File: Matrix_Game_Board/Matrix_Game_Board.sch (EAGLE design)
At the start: 53 parts, among them J1 AVR_SPI_PRG_6NS, J2 AVR_SPI_PRG_6NS, J3 AVR_SPI_PRG_6NS, J4 AVR_SPI_PRG_6NS

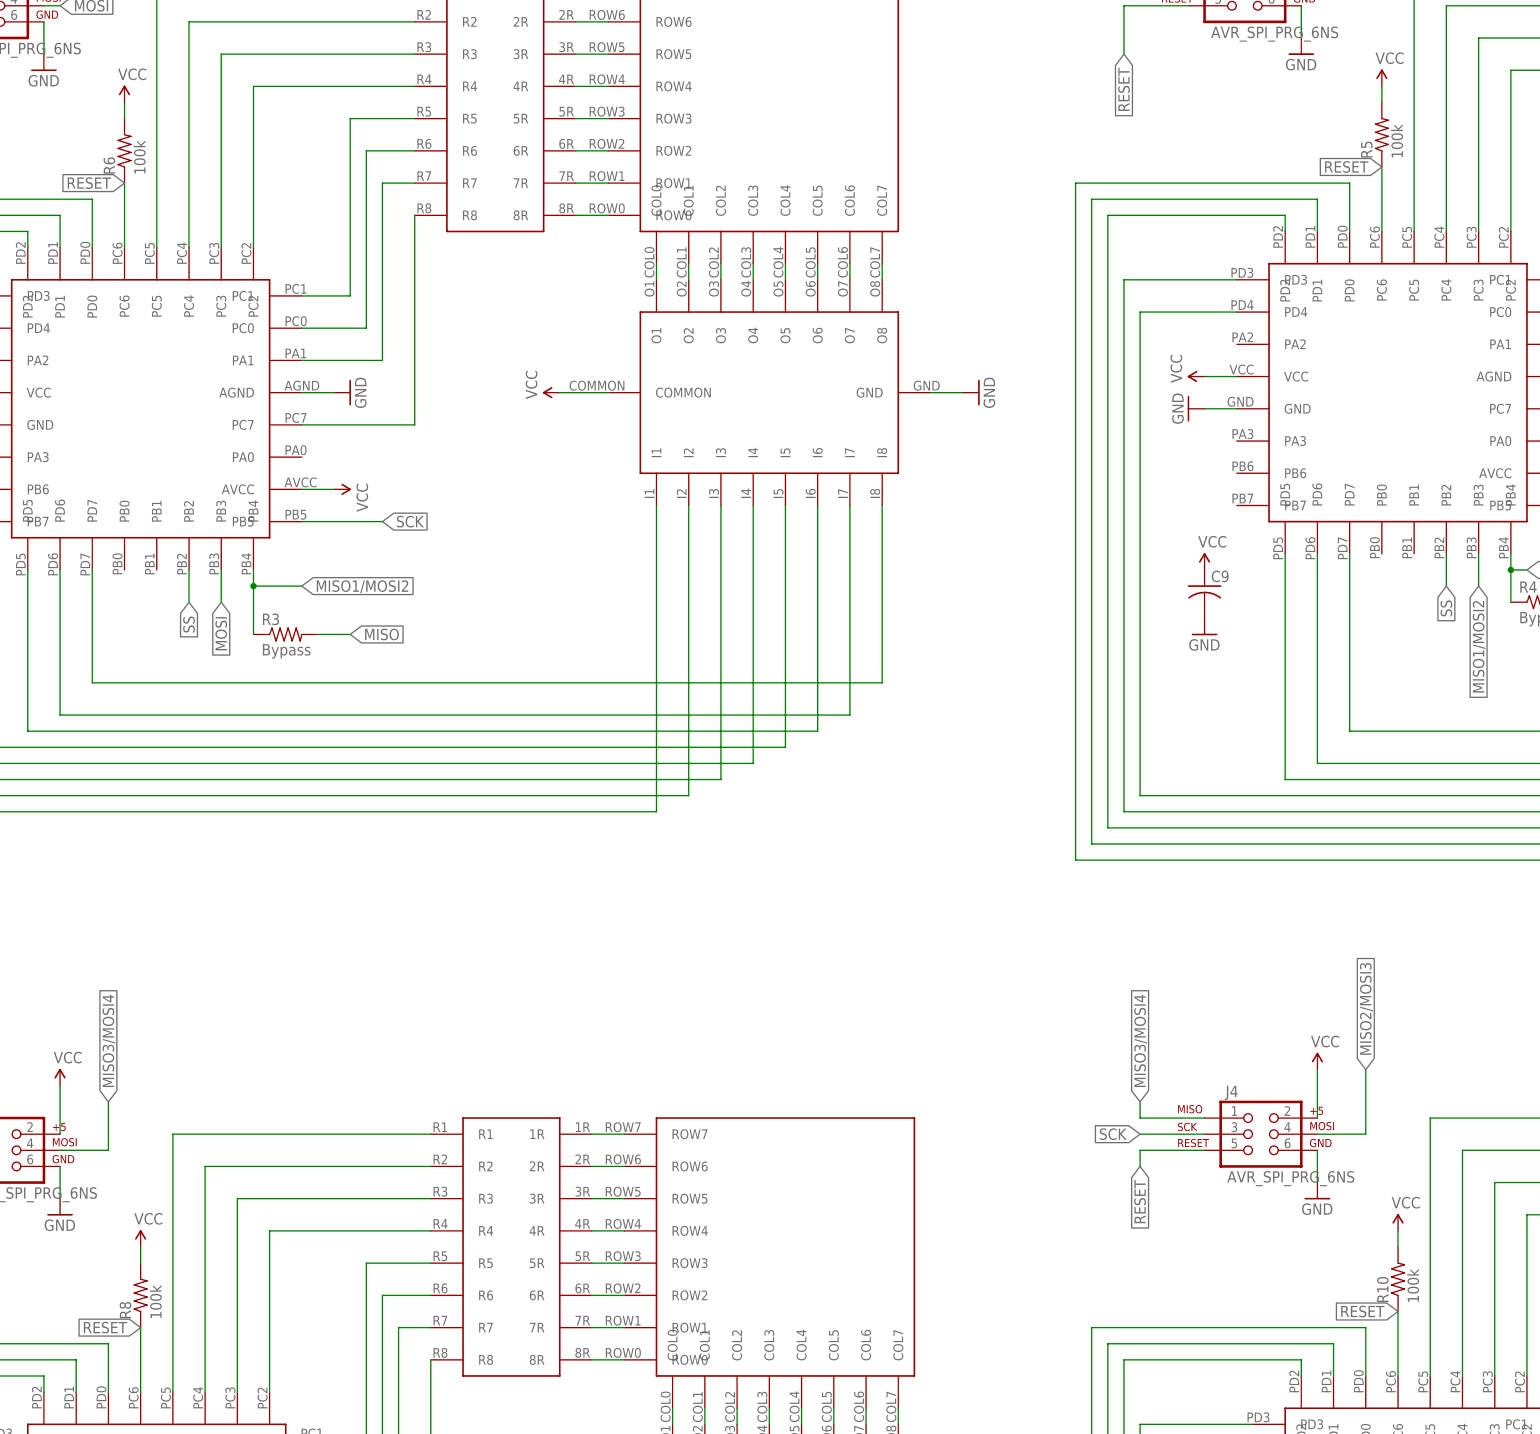
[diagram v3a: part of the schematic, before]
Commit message: Changed resistors to 0603 on gamer PCB
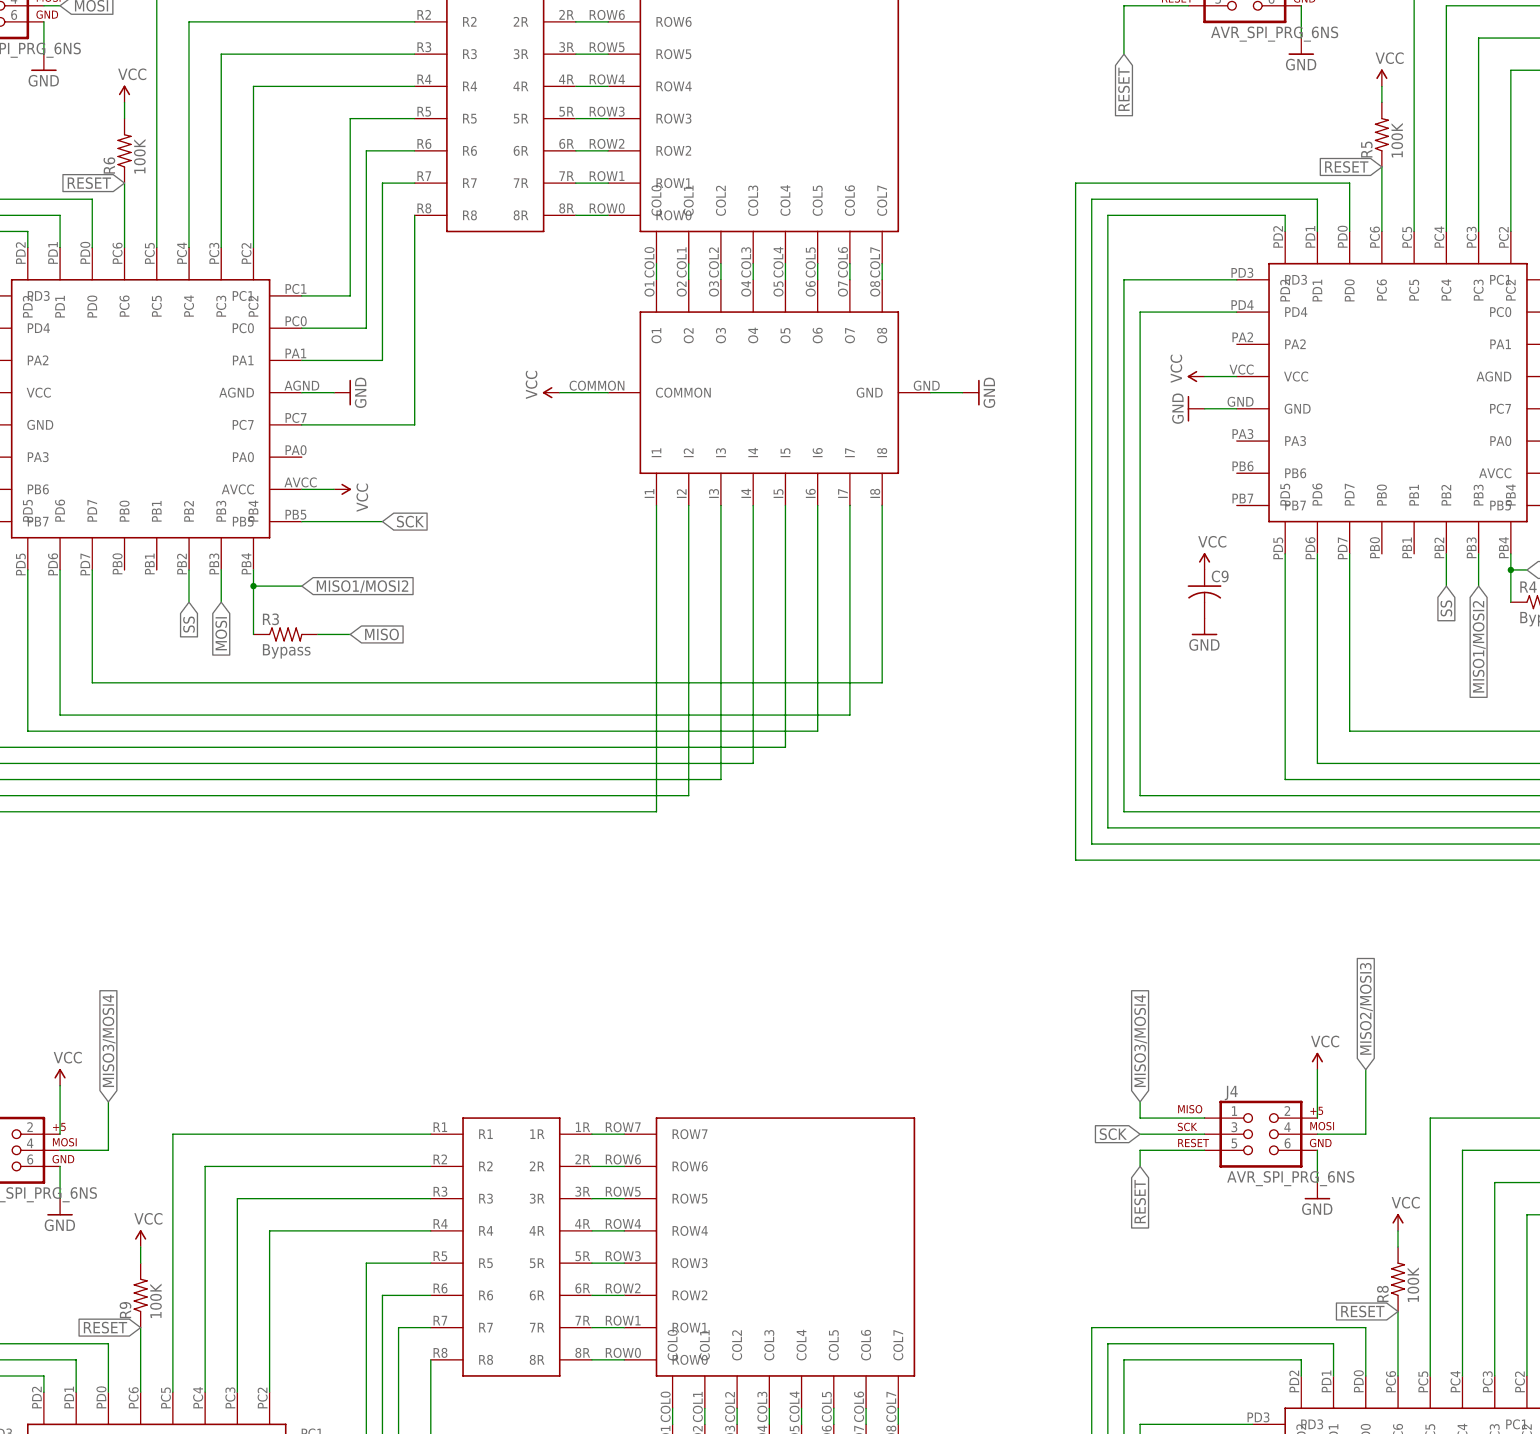
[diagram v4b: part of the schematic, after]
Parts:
- removed R10: 100k, resistor:R-US_R0805
- added R9: 100K, resistor:R-US_R0603
- R3, R4: device resistor:R-US_R0805 -> resistor:R-US_R0603
- R5, R6, R8: value 100k -> 100K; device resistor:R-US_R0805 -> resistor:R-US_R0603
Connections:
- net RESET: now also R9.1; no longer R10.1
- net VCC: now also R9.2; no longer R10.2
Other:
- moved on the sheet: R8
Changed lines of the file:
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@@
 <part name="GND23" library="SparkFun-Aesthetics" deviceset="GND" device=""/>
 <part name="GND26" library="SparkFun-Aesthetics" deviceset="GND" device=""/>
-<part name="R3" library="resistor" deviceset="R-US_" device="R0805" value="Bypass"/>
-<part name="R6" library="resistor" deviceset="R-US_" device="R0805" value="100k"/>
 <part name="SUPPLY22" library="SparkFun-Aesthetics" deviceset="VCC" device=""/>
 <part name="U$25" library="ScottSilver" deviceset="LM386" device=""/>
@@
 <part name="GND8" library="SparkFun-Aesthetics" deviceset="GND" device=""/>
 <part name="SUPPLY8" library="SparkFun-Aesthetics" deviceset="VCC" device=""/>
-<part name="R4" library="resistor" deviceset="R-US_" device="R0805" value="Bypass"/>
-<part name="R5" library="resistor" deviceset="R-US_" device="R0805" value="100k"/>
 <part name="SUPPLY9" library="SparkFun-Aesthetics" deviceset="VCC" device=""/>
 <part name="U$8" library="ScottSilver" deviceset="8X8_LED_MATRIX" device=""/>
@@
 <part name="GND12" library="SparkFun-Aesthetics" deviceset="GND" device=""/>
 <part name="SUPPLY13" library="SparkFun-Aesthetics" deviceset="VCC" device=""/>
-<part name="R8" library="resistor" deviceset="R-US_" device="R0805" value="100k"/>
 <part name="SUPPLY14" library="SparkFun-Aesthetics" deviceset="VCC" device=""/>
 <part name="U$13" library="ScottSilver" deviceset="8X8_LED_MATRIX" device=""/>
@@
 <part name="GND16" library="SparkFun-Aesthetics" deviceset="GND" device=""/>
 <part name="SUPPLY24" library="SparkFun-Aesthetics" deviceset="VCC" device=""/>
-<part name="R10" library="resistor" deviceset="R-US_" device="R0805" value="100k"/>
 <part name="SUPPLY25" library="SparkFun-Aesthetics" deviceset="VCC" device=""/>
 <part name="GND32" library="SparkFun-Aesthetics" deviceset="GND" device=""/>
@@
 <part name="GND38" library="SparkFun-Aesthetics" deviceset="GND" device=""/>
 <part name="GND39" library="SparkFun-Aesthetics" deviceset="GND" device=""/>
+<part name="R3" library="resistor" deviceset="R-US_" device="R0603" value="Bypass"/>
+<part name="R4" library="resistor" deviceset="R-US_" device="R0603" value="Bypass"/>
+<part name="R6" library="resistor" deviceset="R-US_" device="R0603" value="100K"/>
+<part name="R5" library="resistor" deviceset="R-US_" device="R0603" value="100K"/>
+<part name="R8" library="resistor" deviceset="R-US_" device="R0603" value="100K"/>
+<part name="R9" library="resistor" deviceset="R-US_" device="R0603" value="100K"/>
 </parts>
 <sheets>
@@
 <instance part="GND23" gate="1" x="215.9" y="-33.02"/>
 <instance part="GND26" gate="1" x="398.78" y="10.16" rot="MR90"/>
-<instance part="R3" gate="G$1" x="106.68" y="271.78"/>
-<instance part="R6" gate="G$1" x="81.28" y="347.98" rot="R90"/>
 <instance part="SUPPLY22" gate="G$1" x="81.28" y="355.6"/>
 <instance part="U$25" gate="G$1" x="477.52" y="182.88"/>
@@
 <instance part="GND8" gate="1" x="266.7" y="363.22"/>
 <instance part="SUPPLY8" gate="G$1" x="266.7" y="383.54"/>
-<instance part="R4" gate="G$1" x="304.8" y="276.86"/>
-<instance part="R5" gate="G$1" x="279.4" y="350.52" rot="R90"/>
 <instance part="SUPPLY9" gate="G$1" x="279.4" y="358.14"/>
 <instance part="U$8" gate="G$1" x="185.42" y="175.26"/>
@@
 <instance part="GND12" gate="1" x="71.12" y="180.34"/>
 <instance part="SUPPLY13" gate="G$1" x="71.12" y="200.66"/>
-<instance part="R8" gate="G$1" x="83.82" y="167.64" rot="R90"/>
 <instance part="SUPPLY14" gate="G$1" x="83.82" y="175.26"/>
 <instance part="U$13" gate="G$1" x="383.54" y="177.8"/>
@@
 <instance part="GND16" gate="1" x="269.24" y="182.88"/>
 <instance part="SUPPLY24" gate="G$1" x="269.24" y="203.2"/>
-<instance part="R10" gate="G$1" x="281.94" y="170.18" rot="R90"/>
 <instance part="SUPPLY25" gate="G$1" x="281.94" y="177.8"/>
 <instance part="GND32" gate="1" x="452.12" y="27.94" rot="R270"/>
@@
 <instance part="GND38" gate="1" x="436.88" y="-55.88"/>
 <instance part="GND39" gate="1" x="436.88" y="-81.28"/>
+<instance part="R3" gate="G$1" x="106.68" y="271.78"/>
+<instance part="R4" gate="G$1" x="304.8" y="276.86"/>
+<instance part="R6" gate="G$1" x="81.28" y="347.98" rot="R90"/>
+<instance part="R5" gate="G$1" x="279.4" y="350.52" rot="R90"/>
+<instance part="R8" gate="G$1" x="281.94" y="170.18" rot="R90"/>
+<instance part="R9" gate="G$1" x="83.82" y="167.64" rot="R90"/>
 </instances>
 <busses>
@@
 </segment>
 <segment>
-<pinref part="R6" gate="G$1" pin="2"/>
 <pinref part="SUPPLY22" gate="G$1" pin="VCC"/>
 <wire x1="81.28" y1="355.6" x2="81.28" y2="353.06" width="0.1524" layer="91"/>
+<pinref part="R6" gate="G$1" pin="2"/>
 </segment>
 <segment>
@@
 </segment>
 <segment>
-<pinref part="R5" gate="G$1" pin="2"/>
 <pinref part="SUPPLY9" gate="G$1" pin="VCC"/>
 <wire x1="279.4" y1="358.14" x2="279.4" y2="355.6" width="0.1524" layer="91"/>
+<pinref part="R5" gate="G$1" pin="2"/>
 </segment>
 <segment>
@@
 </segment>
 <segment>
-<pinref part="R8" gate="G$1" pin="2"/>
 <pinref part="SUPPLY14" gate="G$1" pin="VCC"/>
 <wire x1="83.82" y1="175.26" x2="83.82" y2="172.72" width="0.1524" layer="91"/>
+<pinref part="R9" gate="G$1" pin="2"/>
 </segment>
 <segment>
@@
 </segment>
 <segment>
-<pinref part="R10" gate="G$1" pin="2"/>
 <pinref part="SUPPLY25" gate="G$1" pin="VCC"/>
 <wire x1="281.94" y1="177.8" x2="281.94" y2="175.26" width="0.1524" layer="91"/>
+<pinref part="R8" gate="G$1" pin="2"/>
 </segment>
 <segment>
@@
 <wire x1="83.82" y1="152.4" x2="83.82" y2="162.56" width="0.1524" layer="91"/>
 <label x="83.82" y="162.56" size="1.778" layer="95" rot="R180" xref="yes"/>
-<pinref part="R8" gate="G$1" pin="1"/>
+<pinref part="R9" gate="G$1" pin="1"/>
 </segment>
 <segment>
@@
 <wire x1="281.94" y1="154.94" x2="281.94" y2="165.1" width="0.1524" layer="91"/>
 <label x="281.94" y="165.1" size="1.778" layer="95" rot="R180" xref="yes"/>
-<pinref part="R10" gate="G$1" pin="1"/>
+<pinref part="R8" gate="G$1" pin="1"/>
 </segment>
 <segment>
@@
 </segment>
 <segment>
-<pinref part="R3" gate="G$1" pin="2"/>
 <wire x1="111.76" y1="271.78" x2="116.84" y2="271.78" width="0.1524" layer="91"/>
 <label x="116.84" y="271.78" size="1.778" layer="95" xref="yes"/>
-</segment>
-<segment>
-<pinref part="R4" gate="G$1" pin="2"/>
+<pinref part="R3" gate="G$1" pin="2"/>
+</segment>
+<segment>
 <wire x1="309.88" y1="276.86" x2="314.96" y2="276.86" width="0.1524" layer="91"/>
 <label x="314.96" y="276.86" size="1.778" layer="95" xref="yes"/>
+<pinref part="R4" gate="G$1" pin="2"/>
 </segment>
 <segment>
@@
 <pinref part="U$9" gate="G$1" pin="PB4"/>
 <wire x1="101.6" y1="271.78" x2="101.6" y2="279.4" width="0.1524" layer="91"/>
-<pinref part="R3" gate="G$1" pin="1"/>
 <wire x1="101.6" y1="279.4" x2="101.6" y2="281.94" width="0.1524" layer="91"/>
 <wire x1="101.6" y1="279.4" x2="109.22" y2="279.4" width="0.1524" layer="91"/>
 <junction x="101.6" y="279.4"/>
 <label x="109.22" y="279.4" size="1.778" layer="95" xref="yes"/>
+<pinref part="R3" gate="G$1" pin="1"/>
 </segment>
 <segment>
@@
 <pinref part="U$6" gate="G$1" pin="PB4"/>
 <wire x1="299.72" y1="276.86" x2="299.72" y2="281.94" width="0.1524" layer="91"/>
-<pinref part="R4" gate="G$1" pin="1"/>
 <wire x1="299.72" y1="281.94" x2="299.72" y2="284.48" width="0.1524" layer="91"/>
 <wire x1="299.72" y1="281.94" x2="302.26" y2="281.94" width="0.1524" layer="91"/>
 <junction x="299.72" y="281.94"/>
 <label x="302.26" y="281.94" size="1.778" layer="95" xref="yes"/>
-</segment>
-<segment>
+<pinref part="R4" gate="G$1" pin="1"/>
+</segment>
+<segment>

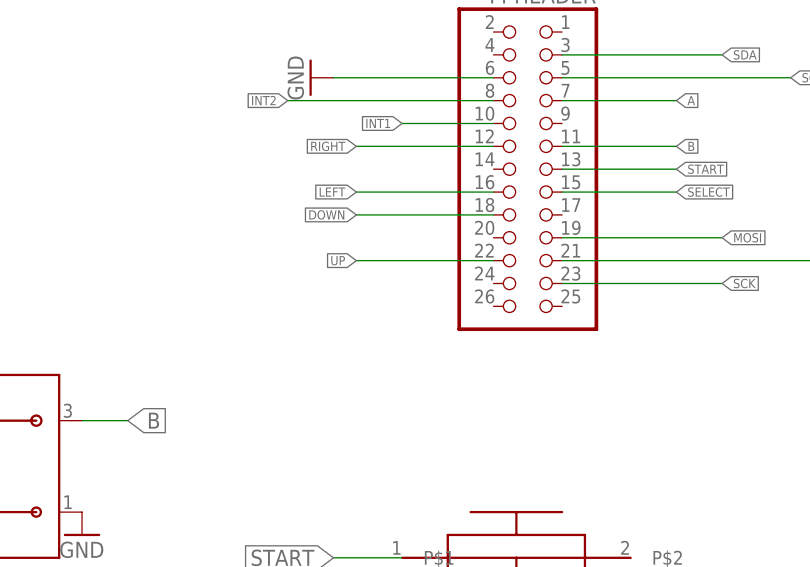
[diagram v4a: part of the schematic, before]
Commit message: Inverted bottom row of matrices, routed CS, added ground plane
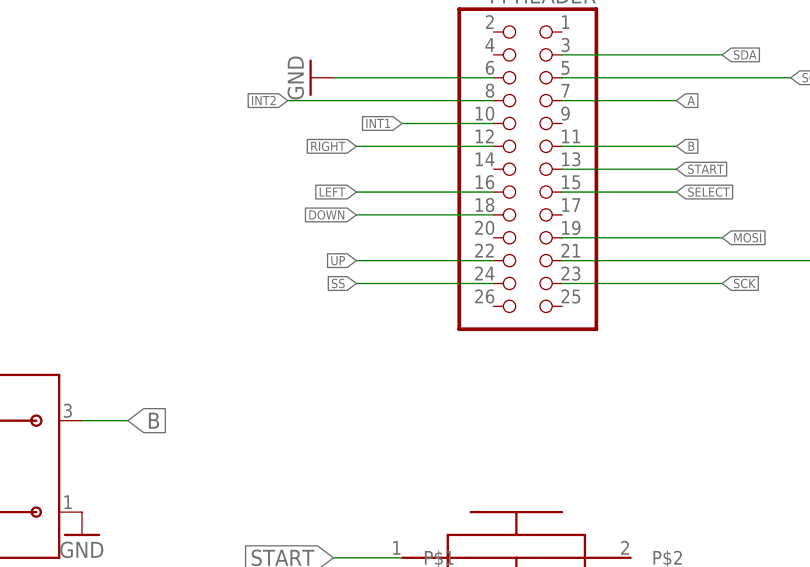
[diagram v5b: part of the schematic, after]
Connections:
- net SS: now also PI-HEADER.24
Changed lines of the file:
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@@
 <label x="292.1" y="99.06" size="1.778" layer="95" rot="R270" xref="yes"/>
+</segment>
+<segment>
+<pinref part="PI-HEADER" gate="A" pin="24"/>
+<wire x1="419.1" y1="-12.7" x2="403.86" y2="-12.7" width="0.1524" layer="91"/>
+<label x="403.86" y="-12.7" size="1.016" layer="95" rot="R180" xref="yes"/>
 </segment>
 </net>
